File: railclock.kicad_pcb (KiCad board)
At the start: 2 copper layers, 98.6 x 99.6 mm, 176 parts, among them J1 Conn_01x02_Pin, J10 Conn_01x04_MountingPin, J11 Conn_01x04_MountingPin, J12 Conn_01x04_MountingPin, J13 Conn_01x04_MountingPin, J14 Conn_01x04_MountingPin, J15 Conn_01x03_MountingPin, J16 Barrel_Jack_Switch, J3 Conn_01x04_MountingPin, J4 USB_C_Receptacle_USB2.0_14P, J5 Conn_01x03_MountingPin, J6 Conn_01x03_MountingPin, J7 Conn_01x03_MountingPin, J8 Conn_01x03_MountingPin, J9 Conn_01x04_MountingPin, K1 G6K-2, K2 G6K-2, K3 G6K-2, K4 G6K-2, K6 G6K-2, Q1 NPN, Q2 NPN, Q3 NPN, Q4 NPN, Q5 NPN, SW1 SW_SPST, SW2 SW_DPDT_x2, U1 MCP7940N-xST, U11 MAX811TEUS-T, U12 MCP4728, U2 MCP73832-2-OT, U4 ESP32-C6-WROOM-1, U5 DRV8870DDA, U6 PAM2421, U8 BQ24296MRGET, U9 PCF8574RGTR, Y2 Crystal_GND3

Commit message: Fix issues with first version
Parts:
- removed D3, D4, D5, D7, D8: D, Diode_SMD:D_MiniMELF
- removed K1, K2, K3, K4, K6: G6K-2, Relay_SMD:Relay_DPDT_Omron_G6K-2F-Y
- removed Q1, Q2, Q3, Q4, Q5: NPN, Package_TO_SOT_SMD:SOT-23
- removed R54, R55, R56, R57, R58, R59, R60, R61, R62, R63, R64, R77, R78, R79, R80, R81: R, Resistor_SMD:R_0805_2012Metric
- added C32: C, Capacitor_SMD:C_0805_2012Metric, F.Cu at (75.2, 111.2)
- added C33: C, Capacitor_SMD:C_0805_2012Metric, F.Cu at (125.4, 31.9)
- added C34: C, Capacitor_SMD:C_0805_2012Metric, F.Cu at (123.5, 46.2)
- added C35: C, Capacitor_SMD:C_0805_2012Metric, F.Cu at (123.6, 60.4)
- added C36: C, Capacitor_SMD:C_0805_2012Metric, F.Cu at (123.7, 74.8)
- added C37: C, Capacitor_SMD:C_0805_2012Metric, F.Cu at (123.7, 89.0)
- added J2: Conn_01x03_MountingPin, Connector_JST:JST_PH_S3B-PH-SM4-TB_1x03-1MP_P2.00mm_Horizontal, F.Cu at (115.2, 28.6)
- added R22: R, Resistor_SMD:R_0805_2012Metric, F.Cu at (117.9, 38.8)
- added U10: 74AHC1G04, Package_TO_SOT_SMD:SOT-23-5, F.Cu at (73.2, 108.1)
- added U13: BTS5012SDA, Package_TO_SOT_SMD:TO-252-4, F.Cu at (125.4, 36.7)
- added U14: BTS5012SDA, Package_TO_SOT_SMD:TO-252-4, F.Cu at (125.3, 51.1)
- added U15: BTS5012SDA, Package_TO_SOT_SMD:TO-252-4, F.Cu at (125.4, 65.3)
- added U16: BTS5012SDA, Package_TO_SOT_SMD:TO-252-4, F.Cu at (125.6, 79.8)
- added U17: BTS5012SDA, Package_TO_SOT_SMD:TO-252-4, F.Cu at (125.6, 93.8)
- R48, R50: moved to F.Cu
- moved R53 46.6 mm to (117.9, 96.0), turned to -90 degrees
- moved R52 44.0 mm to (115.7, 95.1), turned to -90 degrees
- moved R48 41.0 mm to (115.5, 66.6), turned to -90 degrees
- moved R49 38.5 mm to (117.8, 67.5), turned to -90 degrees
- moved R50 27.3 mm to (115.7, 81.2), turned to -90 degrees
- moved R47 18.6 mm to (117.9, 53.4), turned to -90 degrees
- moved H4 18.6 mm to (130.8, 27.8)
- moved R45 16.3 mm to (115.6, 52.5), turned to -90 degrees
- moved R51 13.2 mm to (118.0, 82.1), turned to -90 degrees
- moved R5 8.42 mm to (103.8, 48.3)
- moved R6 7.81 mm to (100.8, 46.9), turned to 90 degrees
- moved R46 6.40 mm to (115.6, 37.8), turned to -90 degrees
- moved R13 4.23 mm to (71.5, 111.1)
- moved R2 4.14 mm to (78.9, 71.9)
- moved C5 4.00 mm to (77.8, 59.4)
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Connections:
- J10 pad 2: Net-(J10-Pin_2) -> +12V
- J10 pad 3: +12V -> +3.3V
- J11 pad 2: Net-(J11-Pin_2) -> +12V
- J11 pad 3: +12V -> +3.3V
- J12 pad 2: Net-(J12-Pin_2) -> +12V
- J12 pad 3: +12V -> +3.3V
- J13 pad 2: Net-(J13-Pin_2) -> +12V
- J13 pad 3: +12V -> +3.3V
- J14 pad 2: Net-(J14-Pin_2) -> +12V
- J14 pad 3: +12V -> +3.3V
- R45 pad 1: Net-(Q1-B) -> OUT1
- R45 pad 2: OUT0 -> Net-(J10-Pin_1)
- R47 pad 1: +3.3V -> Net-(U14-IS)
- R47 pad 2: Net-(J11-Pin_2) -> GND
- R48 pad 1: MOTOR_OUT2 -> OUT2
- R48 pad 2: Net-(K1-Pad5) -> Net-(J12-Pin_1)
- R49 pad 1: GND -> Net-(U15-IS)
- R49 pad 2: Net-(K1-Pad5) -> GND
- R50 pad 1: MOTOR_OUT1 -> OUT3
- R50 pad 2: Net-(K1-Pad4) -> Net-(J13-Pin_1)
- R51 pad 1: +3.3V -> Net-(U16-IS)
- R51 pad 2: Net-(K1-Pad4) -> GND
- R52 pad 1: OUT1 -> OUT4
- R52 pad 2: Net-(J10-Pin_1) -> Net-(J14-Pin_1)
- R53 pad 1: +3.3V -> Net-(U17-IS)
- R53 pad 2: Net-(J10-Pin_2) -> GND
- U3 pad 1: VBUS_ENABLE -> Net-(U3-~{EN})
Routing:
- net VPP: track 249.1 -> 146.6 mm, vias 9 -> 3
- net Net-(K1-Pad5): track 90.1 -> 0.00 mm, vias 6 -> 0
- net Net-(K1-Pad4): track 79.5 -> 0.00 mm, vias 5 -> 0
- net +12V: track 199.8 -> 251.6 mm, vias 0 -> 2
- net DC_JACK_PRESENT: track 0.03 -> 41.0 mm
- net +3.3V: track 473.2 -> 443.8 mm, vias 20 -> 23
- net GND: track 251.1 -> 280.4 mm, vias 102 -> 115
- net Net-(J11-Pin_2): track 20.3 -> 0.00 mm
- net Net-(J10-Pin_2): track 19.8 -> 0.00 mm
- net Net-(J13-Pin_2): track 18.8 -> 0.00 mm
- net Net-(J14-Pin_2): track 18.7 -> 0.00 mm
- net Net-(J12-Pin_2): track 18.6 -> 0.00 mm
- net BOOT1: track 13.6 -> 31.2 mm, vias 0 -> 2
- net +BATT: track 196.5 -> 213.4 mm, vias 4 -> 8
- net Net-(J10-Pin_1): track 16.2 -> 29.5 mm
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
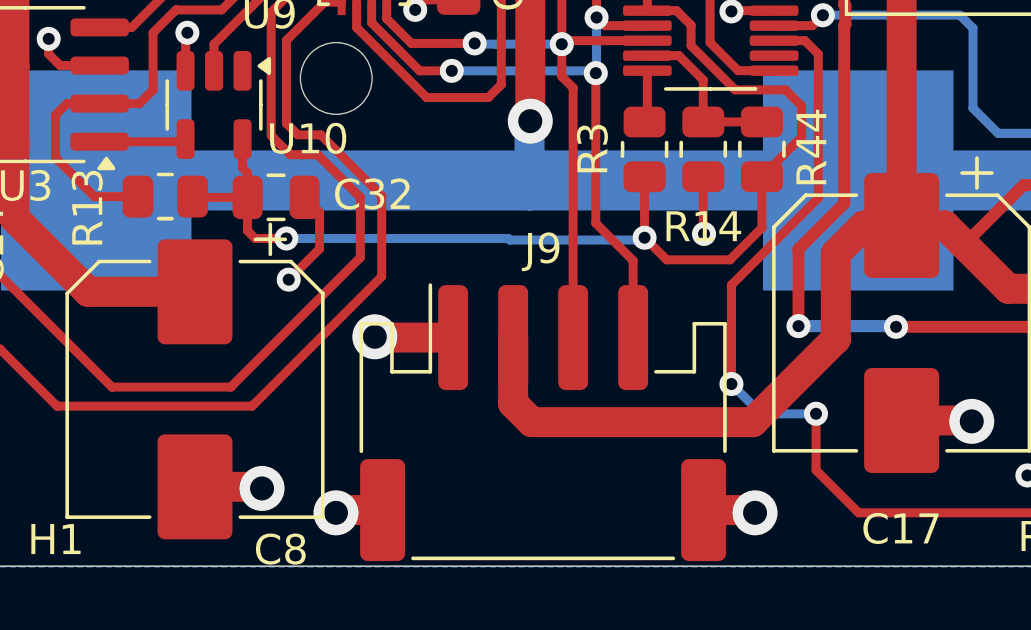
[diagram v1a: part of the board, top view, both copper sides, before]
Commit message: Add option to choose which volatage is avaialble on the I2C connector
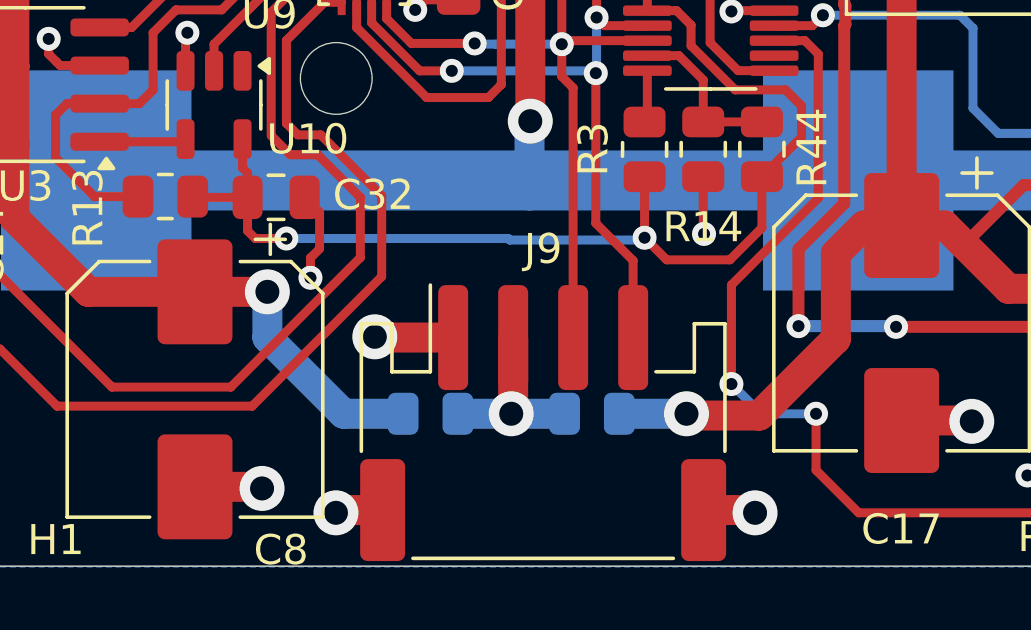
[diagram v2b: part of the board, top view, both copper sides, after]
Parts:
- added R54: R, Resistor_SMD:R_0805_2012Metric, B.Cu at (85.7, 118.4)
- added R55: R, Resistor_SMD:R_0805_2012Metric, B.Cu at (80.4, 118.4)
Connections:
- J9 pad 2: VPP -> Net-(J9-Pin_2)
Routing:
- net +5V: track 119.9 -> 129.4 mm, vias 2 -> 3
- net VPP: track 146.6 -> 139.8 mm, vias 3 -> 4
- net Net-(J9-Pin_2): track 0.00 -> 6.12 mm, vias 0 -> 1

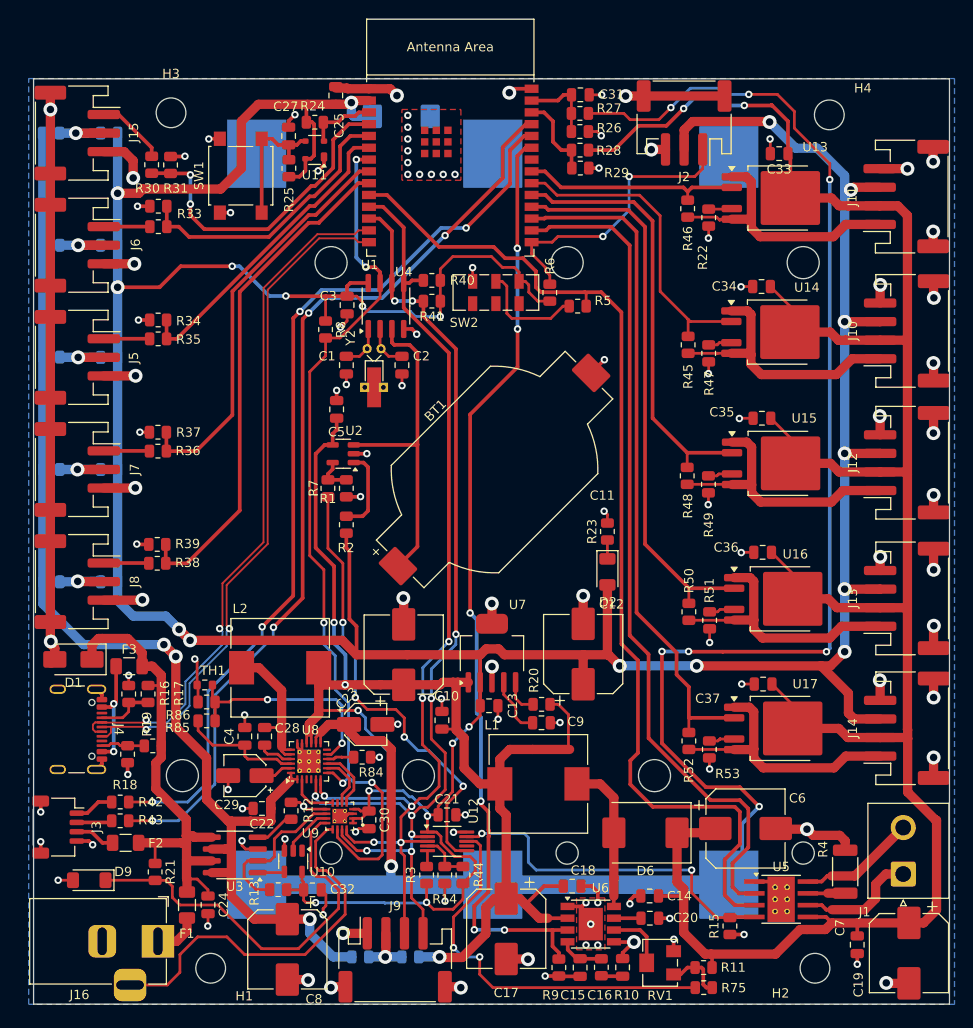
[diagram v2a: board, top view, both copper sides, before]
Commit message: Update board, rewire digital connections
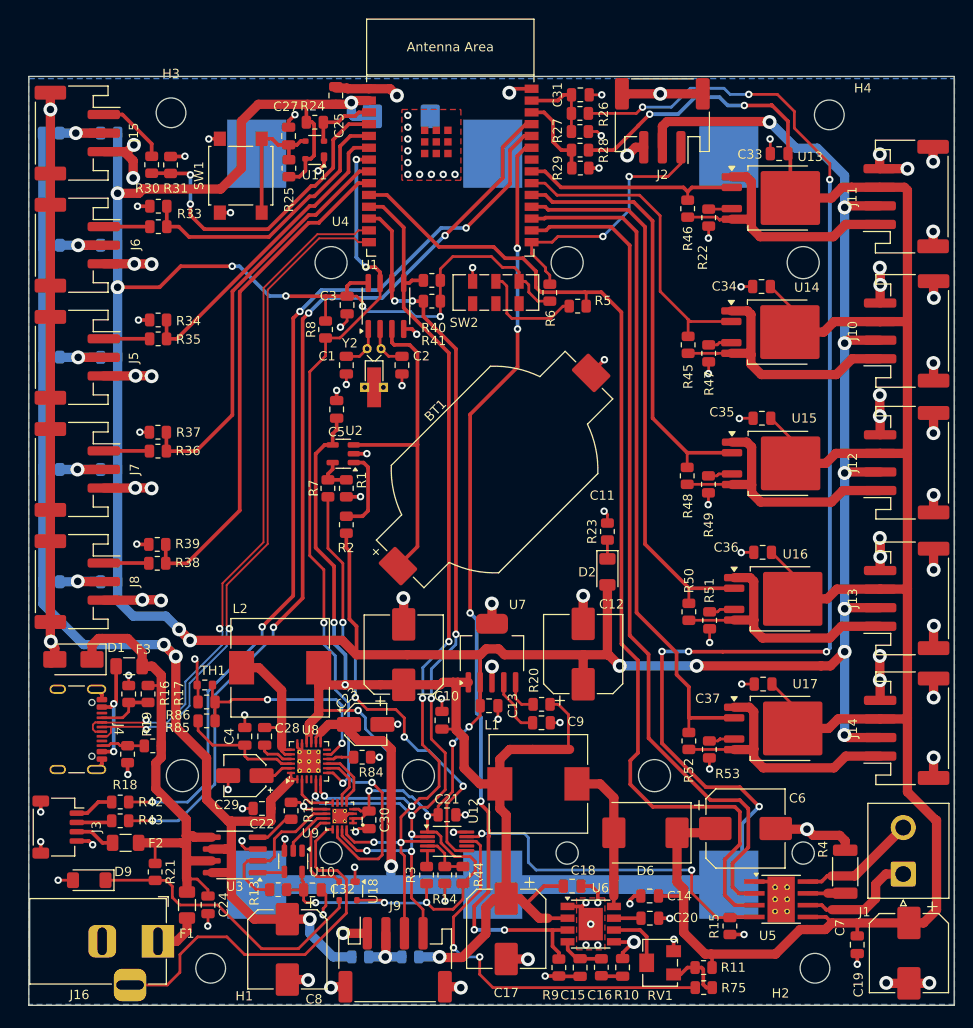
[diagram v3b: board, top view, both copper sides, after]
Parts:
- added U18: MAX811TEUS-T, Package_TO_SOT_SMD:SOT-143, F.Cu at (79.1, 111.3)
- moved J2 2.36 mm to (112.9, 28.4)
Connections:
- J10 pad 2: +12V -> +3.3V
- J10 pad 3: +3.3V -> +12V
- J11 pad 2: +12V -> +3.3V
- J11 pad 3: +3.3V -> +12V
- J12 pad 2: +12V -> +3.3V
- J12 pad 3: +3.3V -> +12V
- J13 pad 2: +12V -> +3.3V
- J13 pad 3: +3.3V -> +12V
- J14 pad 2: +12V -> +3.3V
- J14 pad 3: +3.3V -> +12V
- U9 pad 12: Net-(D9-K) -> Net-(U18-~{RESET})
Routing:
- net GND: track 280.1 -> 301.7 mm, vias 115 -> 127
- net Net-(D9-K): track 42.6 -> 31.5 mm
- net Net-(U18-~{RESET}): track 0.00 -> 9.73 mm
- net +3.3V: track 443.8 -> 452.1 mm, vias 23 -> 25
- net +12V: track 251.6 -> 254.1 mm
- net BOOT1: track 31.2 -> 28.8 mm
- net DC_JACK_PRESENT: track 41.0 -> 41.8 mm
- net +BATT: track 213.4 -> 212.8 mm
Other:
- board size 98.6 x 99.6 mm -> 99.6 x 99.9 mm

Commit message: Add transils fix vbus detection
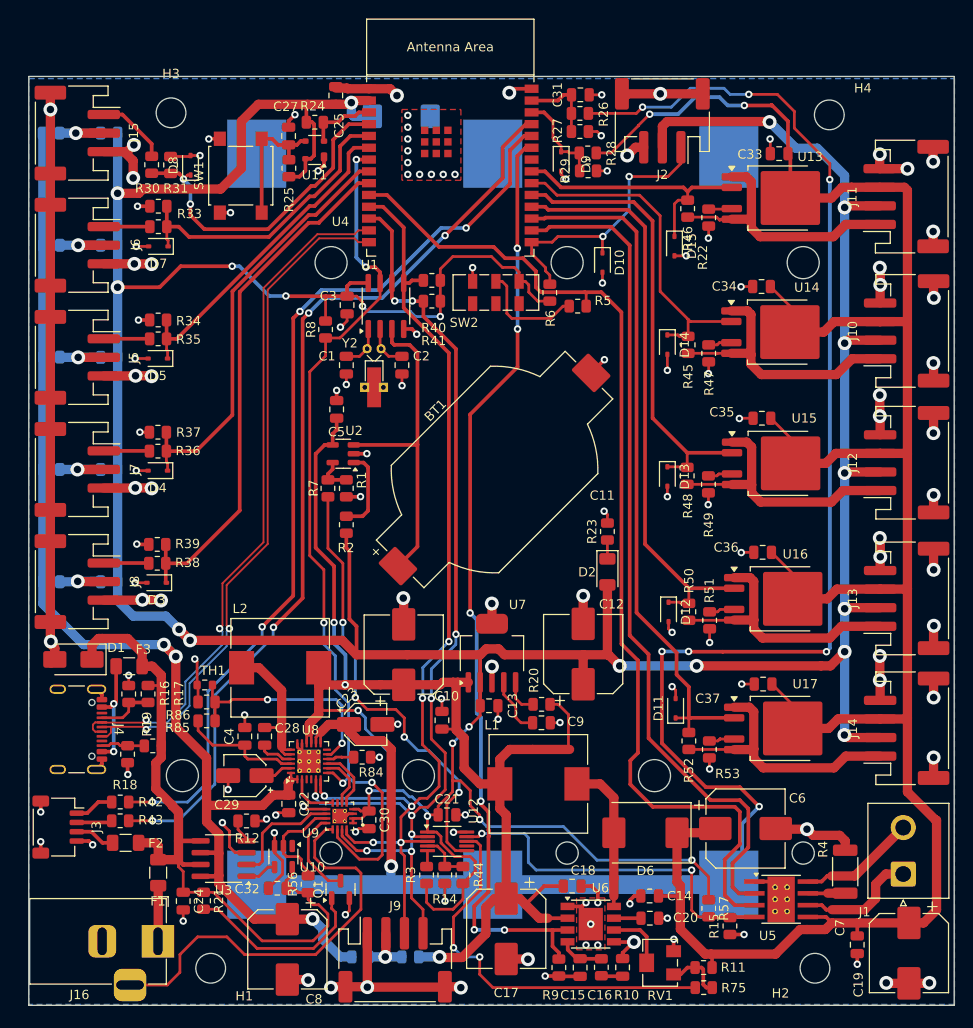
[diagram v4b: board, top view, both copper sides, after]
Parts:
- removed R13: 10k, Resistor_SMD:R_0805_2012Metric
- removed U18: MAX811TEUS-T, Package_TO_SOT_SMD:SOT-143
- added D10: D_Zener, Diode_SMD:D_SOD-323, F.Cu at (106.4, 43.7)
- added D11: D_Zener, Diode_SMD:D_SOD-323, F.Cu at (114.3, 91.6)
- added D12: D_Zener, Diode_SMD:D_SOD-323, F.Cu at (113.5, 81.2)
- added D13: D_Zener, Diode_SMD:D_SOD-323, F.Cu at (113.4, 66.7)
- added D14: D_Zener, Diode_SMD:D_SOD-323, F.Cu at (113.4, 52.5)
- added D15: D_Zener, Diode_SMD:D_SOD-323, F.Cu at (114.2, 41.9)
- added D3: D_Zener, Diode_SMD:D_SOD-323, F.Cu at (58.5, 78.1)
- added D4: D_Zener, Diode_SMD:D_SOD-323, F.Cu at (58.6, 66.0)
- added D5: D_Zener, Diode_SMD:D_SOD-323, F.Cu at (58.6, 54.0)
- added D7: D_Zener, Diode_SMD:D_SOD-323, F.Cu at (58.6, 41.9)
- added D8: D_Zener, Diode_SMD:D_SOD-323, F.Cu at (62.1, 33.2)
- added Q1: Q_NPN_BEC, Package_TO_SOT_SMD:SOT-23, F.Cu at (78.2, 111.1)
- added R56: 100k, Resistor_SMD:R_0805_2012Metric, F.Cu at (74.8, 110.5)
- added R57: R, Resistor_SMD:R_0805_2012Metric, F.Cu at (117.9, 113.1)
- D9: footprint Diode_SMD:D_MiniMELF -> Diode_SMD:D_SOD-323
- moved D9 92.5 mm to (102.0, 32.8), turned to -90 degrees
- moved R21 6.06 mm to (63.5, 112.3)
- moved R12 4.92 mm to (68.1, 103.7), turned to 0 degrees
- moved F1 4.66 mm to (58.6, 109.3)
- moved C32 3.78 mm to (71.4, 111.0), turned to 180 degrees
- moved C22 2.92 mm to (72.7, 101.9), turned to -90 degrees
- moved C24 2.70 mm to (61.3, 112.4)
- moved U3 1.27 mm to (65.7, 107.8)
- moved U10 1.17 mm to (72.1, 107.6)
- moved R29 0.89 mm to (104.9, 33.8)
- moved R28 0.89 mm to (104.8, 31.9)
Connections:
- C32 pad 1: +3.3V -> VBUS
- D9 pad 1: Net-(D9-K) -> ADC1
- R21 pad 2: Net-(D9-K) -> Net-(Q1-B)
- U10 pad 5: +3.3V -> VBUS
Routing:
- net GND: track 301.7 -> 335.3 mm, vias 127 -> 137
- net Net-(D9-K): track 31.5 -> 0.00 mm
- net VBUS: track 54.7 -> 77.4 mm
- net Net-(Q1-B): track 0.00 -> 20.1 mm
- net +3.3V: track 452.1 -> 466.2 mm, vias 25 -> 24
- net VBUS_ENABLE: track 5.53 -> 11.5 mm
- net OUT0: track 23.6 -> 28.6 mm
- net VBUS_FLG: track 16.9 -> 12.6 mm
- net DC_JACK_PRESENT: track 41.8 -> 44.8 mm
- net OUT1: track 34.3 -> 36.6 mm
- net OUT3: track 60.4 -> 62.7 mm
- net ADC3: track 30.4 -> 32.6 mm
- net ADC4: track 33.5 -> 35.7 mm
- net OUT2: track 47.1 -> 49.2 mm
- net ADC5: track 44.1 -> 46.2 mm
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
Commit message: Replace UART connector
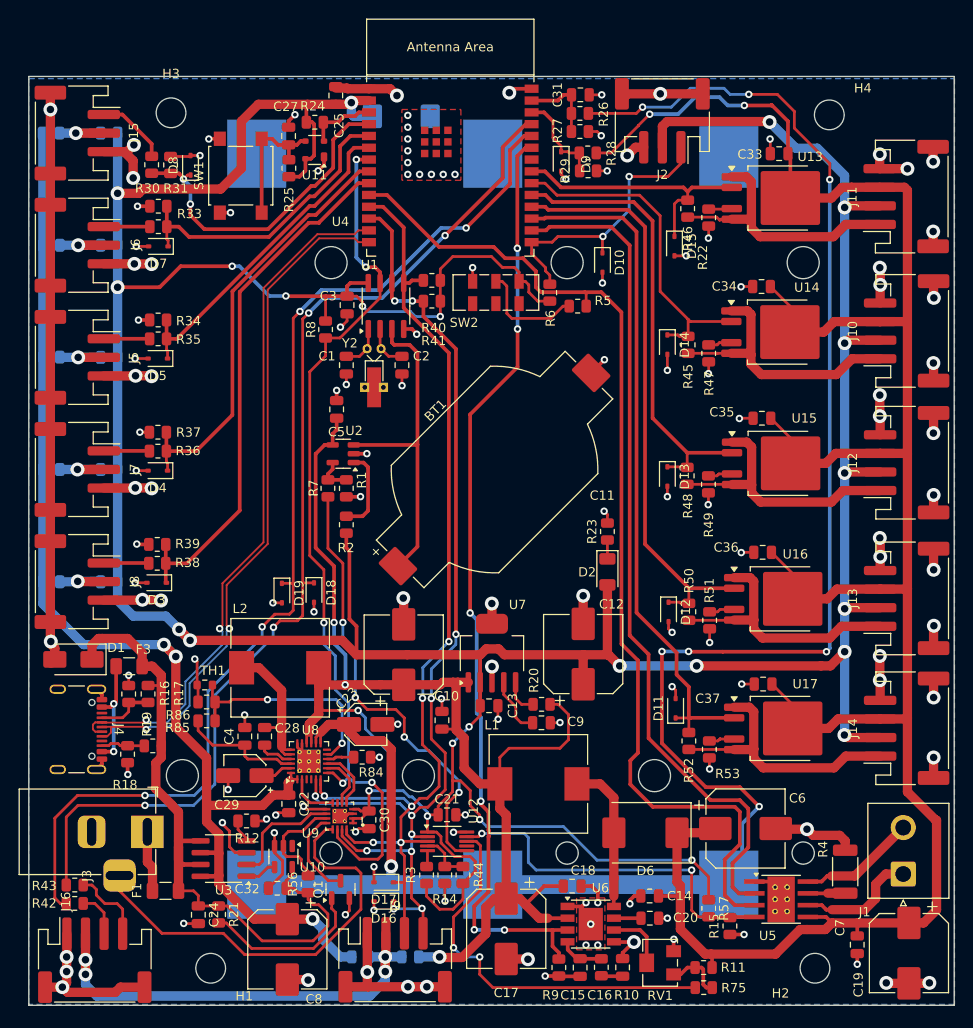
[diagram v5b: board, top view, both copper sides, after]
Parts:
- removed F2: Fuse, Fuse:Fuse_1206_3216Metric
- added D16: D_Zener, Diode_SMD:D_SOD-323, F.Cu at (82.9, 112.4)
- added D17: D_Zener, Diode_SMD:D_SOD-323, F.Cu at (82.9, 110.3)
- added D18: D_Zener, Diode_SMD:D_SOD-323, F.Cu at (75.4, 79.2)
- added D19: D_Zener, Diode_SMD:D_SOD-323, F.Cu at (71.9, 79.2)
- J3: footprint Connector_JST:JST_SH_SM04B-SRSS-TB_1x04-1MP_P1.00mm_Horizontal -> Connector_JST:JST_PH_S4B-PH-SM4-TB_1x04-1MP_P2.00mm_Horizontal
- moved J3 14.9 mm to (51.8, 118.7), turned to 0 degrees
- moved R42 12.0 mm to (49.6, 112.6), turned to 180 degrees
- moved J16 11.8 mm to (57.5, 104.9)
- moved R43 8.46 mm to (49.6, 110.6), turned to 180 degrees
- moved C24 2.19 mm to (62.9, 113.8)
- moved R21 2.19 mm to (65.1, 113.8)
- moved F1 2.10 mm to (59.4, 111.3), turned to 0 degrees
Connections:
- J3 pad 1: Net-(J3-Pin_1) -> GND
- J3 pad 4: GND -> Net-(J3-Pin_4)
- J9 pad 2: Net-(J9-Pin_2) -> Net-(J3-Pin_2)
- R42 pad 1: Net-(J3-Pin_1) -> Net-(J3-Pin_3)
- R43 pad 1: Net-(J3-Pin_2) -> Net-(J3-Pin_4)
- R54 pad 2: Net-(J9-Pin_2) -> Net-(J3-Pin_2)
- R55 pad 2: Net-(J9-Pin_2) -> Net-(J3-Pin_2)
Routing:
- net Net-(J3-Pin_2): track 3.83 -> 50.8 mm, vias 0 -> 4
- net U0RX: track 99.0 -> 119.9 mm
- net U0TX: track 100.1 -> 116.3 mm
- net GND: track 335.3 -> 349.8 mm, vias 137 -> 141
- net Net-(J3-Pin_4): track 0.00 -> 8.32 mm
- net Net-(J9-Pin_2): track 6.12 -> 0.00 mm, vias 1 -> 0
- net Net-(J3-Pin_1): track 4.26 -> 0.00 mm
- net SCL: track 111.4 -> 115.3 mm, vias 9 -> 11
- net VBUS: track 77.4 -> 73.7 mm
- net Net-(Q1-B): track 20.1 -> 17.9 mm
- net DC_JACK_PRESENT: track 44.8 -> 46.3 mm
- net SDA: track 110.9 -> 112.1 mm
- net VPP: track 139.8 -> 138.9 mm
- net Net-(F1-Pad1): track 6.00 -> 6.58 mm
- net Net-(J3-Pin_3): track 4.35 -> 4.92 mm
